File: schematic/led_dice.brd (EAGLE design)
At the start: 39.4 x 58.5 mm, 14 parts, among them U1 ATTINY85-20P, X1 332-02

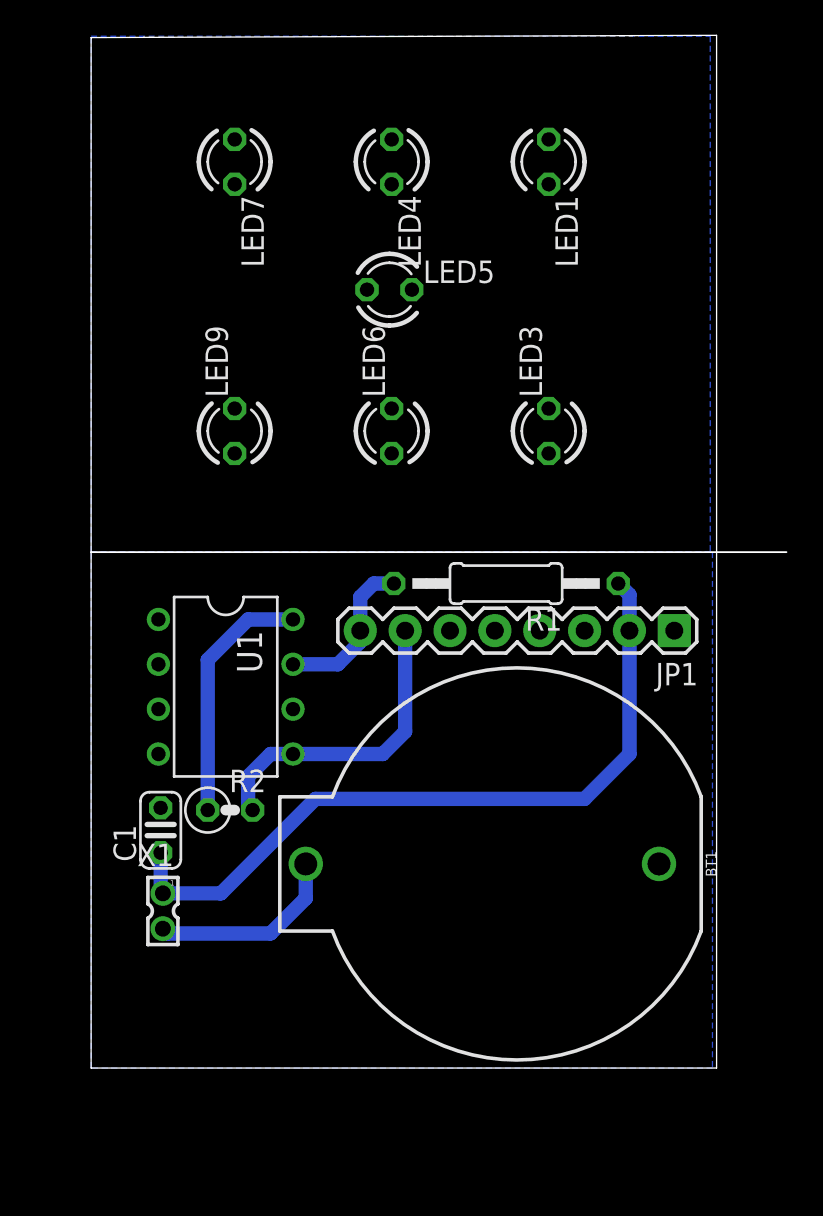
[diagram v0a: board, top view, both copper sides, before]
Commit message: ADXL345 Shake detection added to Sketch + Schematic updated
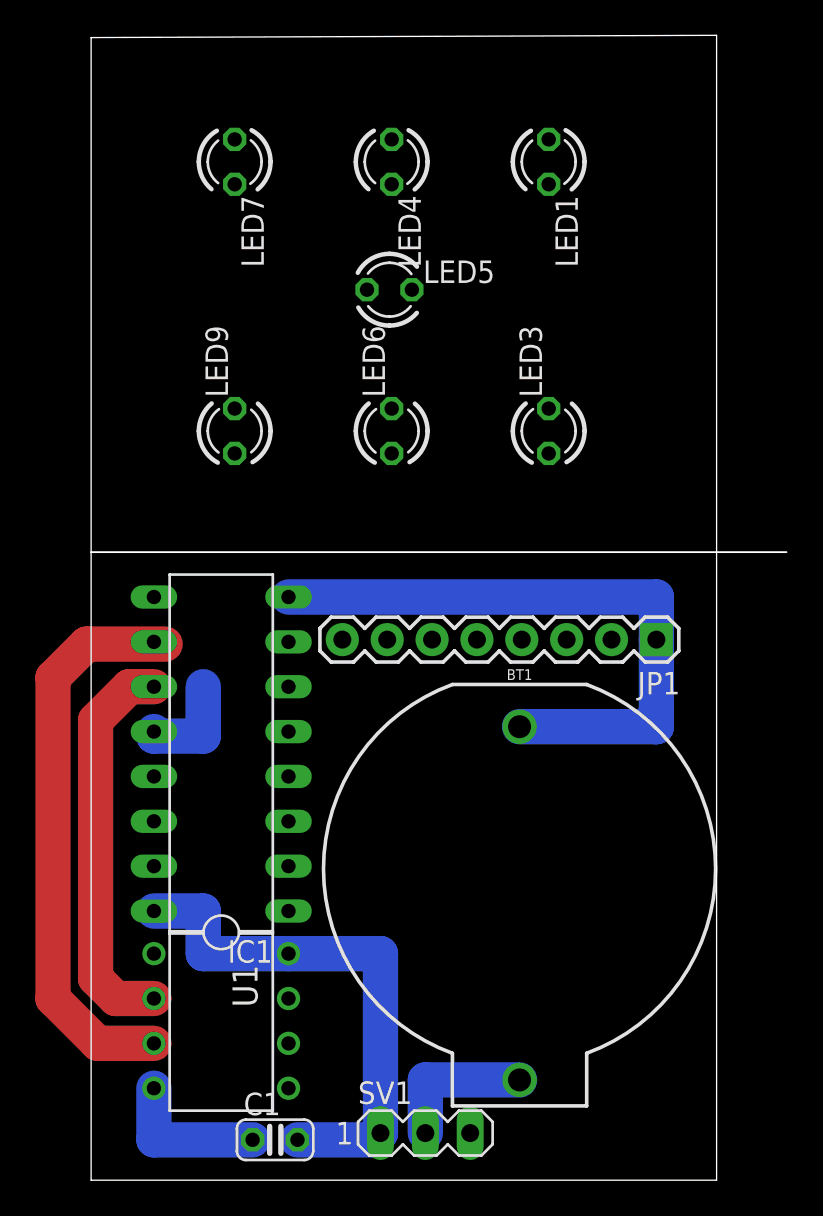
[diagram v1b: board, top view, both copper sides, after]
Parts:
- removed R1: (no value), resistor:0207/12
- removed R2: (no value), resistor:0207/2V
- removed X1: 332-02, con-garry:332-02
- added IC1: 74HC595N, 74xx-eu:DIL16
- added SV1: (no value), con-lstb:MA03-1
- C1: value (none) -> 10nF
- moved U1 18.9 mm to (7.37, 2.67)
- moved C1 18.7 mm to (10.4, -4.06), turned to 0 degrees
- moved JP1 1.14 mm to (32.0, 24.3)
- moved BT1 0.46 mm to (24.3, 11.2), turned to 270 degrees
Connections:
- net SDO renamed N$10
- removed net CS: JP1.3
- new net N$3: IC1.15, LED5.A
- new net N$4: IC1.11, U1.2
- new net N$6: BT1.1, SV1.2
- new net N$8: IC1.12, IC1.14, U1.3
- net GND: now also C1.1, IC1.13, IC1.8, LED5.K; no longer C1.2
- net N$2: now also IC1.1; no longer U1.3
- net N$5: now also IC1.3; no longer U1.2
- net N$7: now also IC1.2; no longer U1.6
- net SCL: no longer R1.2
- net SDA: no longer LED5.K, R2.2
- net VCC: now also C1.2, IC1.10, IC1.16, JP1.3, SV1.1; no longer BT1.1, C1.1, LED5.A, R1.1, R2.1, X1.1, X1.2
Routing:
- net GND: track 0.00 -> 44.4 mm
- net N$8: track 0.00 -> 37.9 mm
- net VCC: track 67.2 -> 30.3 mm
- net N$4: track 0.00 -> 22.5 mm
- net SDA: track 17.7 -> 0.00 mm
- net SCL: track 9.10 -> 0.00 mm
- net N$6: track 0.00 -> 8.34 mm
- removed copper zone on layer 16, net GND
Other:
- board size 39.4 x 58.5 mm -> 39.4 x 64.8 mm
- board text added: "3.80cm"
- board text added: "3.85cm"
